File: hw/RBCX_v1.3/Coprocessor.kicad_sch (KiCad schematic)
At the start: 31 parts

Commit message: Work in progress
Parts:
- IC1: renamed from IC?; footprint RBCX:QFN50P400X400X95-24N -> Package_DFN_QFN:QFN-24-1EP_4x4mm_P0.5mm_EP2.7x2.6mm
- IC2: renamed from IC?; footprint RBCX:QFP50P1600X1600X160-100N_STM32F103VCT6 -> RBCX:LQFN100_14x14mm
- Y2: renamed from Y?; footprint RBCX:SMD-3215_2P -> Crystal:Crystal_SMD_3215-2Pin_3.2x1.5mm
- gave numbers to parts that had none: 28

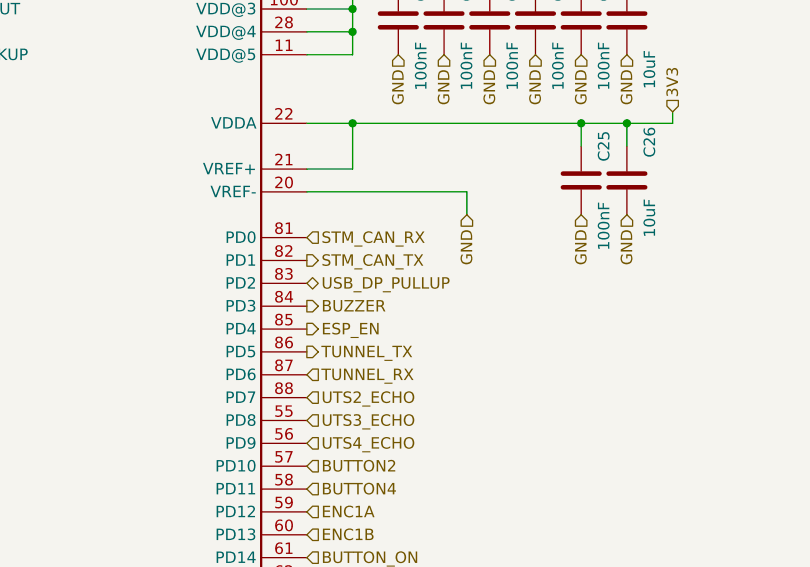
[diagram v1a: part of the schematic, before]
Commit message: New PCB layout
some changes of schema:
- change PD sink AO33772 to AO33771
- remove power switch
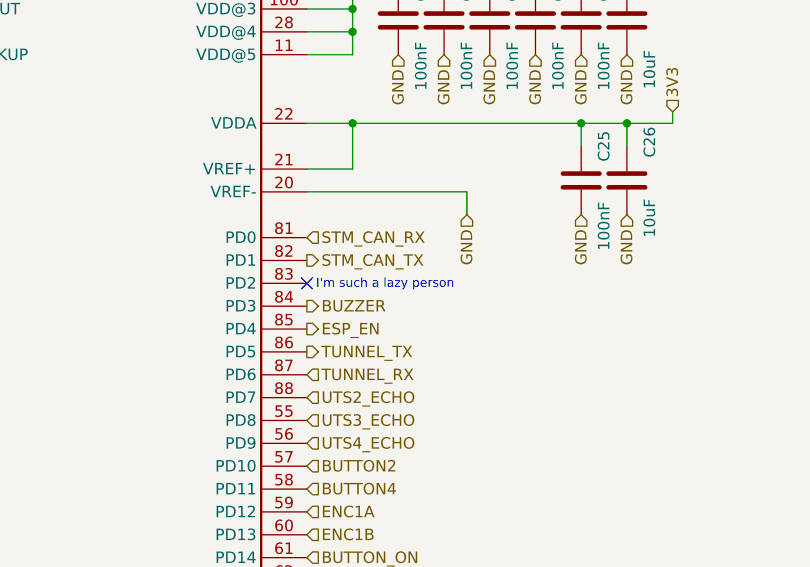
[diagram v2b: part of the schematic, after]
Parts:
- J34: footprint Connector_PinHeader_2.54mm:PinHeader_1x04_P2.54mm_Vertical -> RBCX:PinHeader_1x04_P2.54mm_Vertical
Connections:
- net USB_DP_PULLUP: no longer names the net of IC2.83 (PD2)
- no-connect marks 0 -> 1
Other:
- note added: "I'm such a lazy person"
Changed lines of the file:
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@@
   (junction (at 101.6 33.02) (diameter 0) (color 0 0 0 0)
   )
+  (no_connect (at 91.44 68.58))
   (wire (pts (xy 147.32 147.32) (xy 144.78 147.32))
     (stroke (width 0) (type default) (color 0 0 0 0))
@@
   (wire (pts (xy 116.84 35.56) (xy 116.84 33.02))
     (stroke (width 0) (type default) (color 0 0 0 0))
+  )
+  (text "I'm such a lazy person" (at 92.456 69.342 0)
+    (effects (font (size 1 1)) (justify left bottom))
   )
   (text "v1.3" (at 217.805 191.643 180)
@@
   )
   (hierarchical_label "PWM3B" (shape output) (at 91.44 137.16 0)
-    (effects (font (size 1.27 1.27)) (justify left))
-  )
-  (hierarchical_label "USB_DP_PULLUP" (shape bidirectional) (at 91.44 68.58 0)
     (effects (font (size 1.27 1.27)) (justify left))
   )
@@
       (effects (font (size 1.27 1.27)) (justify left))
     )
-    (property "Footprint" "Connector_PinHeader_2.54mm:PinHeader_1x04_P2.54mm_Vertical" (id 2) (at 243.84 97.79 0)
-      (effects (font (size 1.27 1.27)) hide)
-    )
+    (property "Footprint" "RBCX:PinHeader_1x04_P2.54mm_Vertical" (id 2) (at 243.84 97.79 0)
+      (effects (font (size 1.27 1.27)) hide)
+    )

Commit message: Production files
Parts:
- J34: JLCPCB_CORRECTION (none) -> 0;-3.81;90
- TP12: JLCPCB_IGNORE (none) -> 1
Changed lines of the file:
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@@
+      (effects (font (size 1.27 1.27)) hide)
+    )
+    (property "JLCPCB_IGNORE" "1" (id 4) (at 186.69 54.61 0)
       (effects (font (size 1.27 1.27)) hide)
     )
@@
       (effects (font (size 1.27 1.27)) hide)
     )
+    (property "JLCPCB_CORRECTION" "0;-3.81;90" (id 6) (at 243.84 97.79 0)
+      (effects (font (size 1.27 1.27)) hide)
+    )

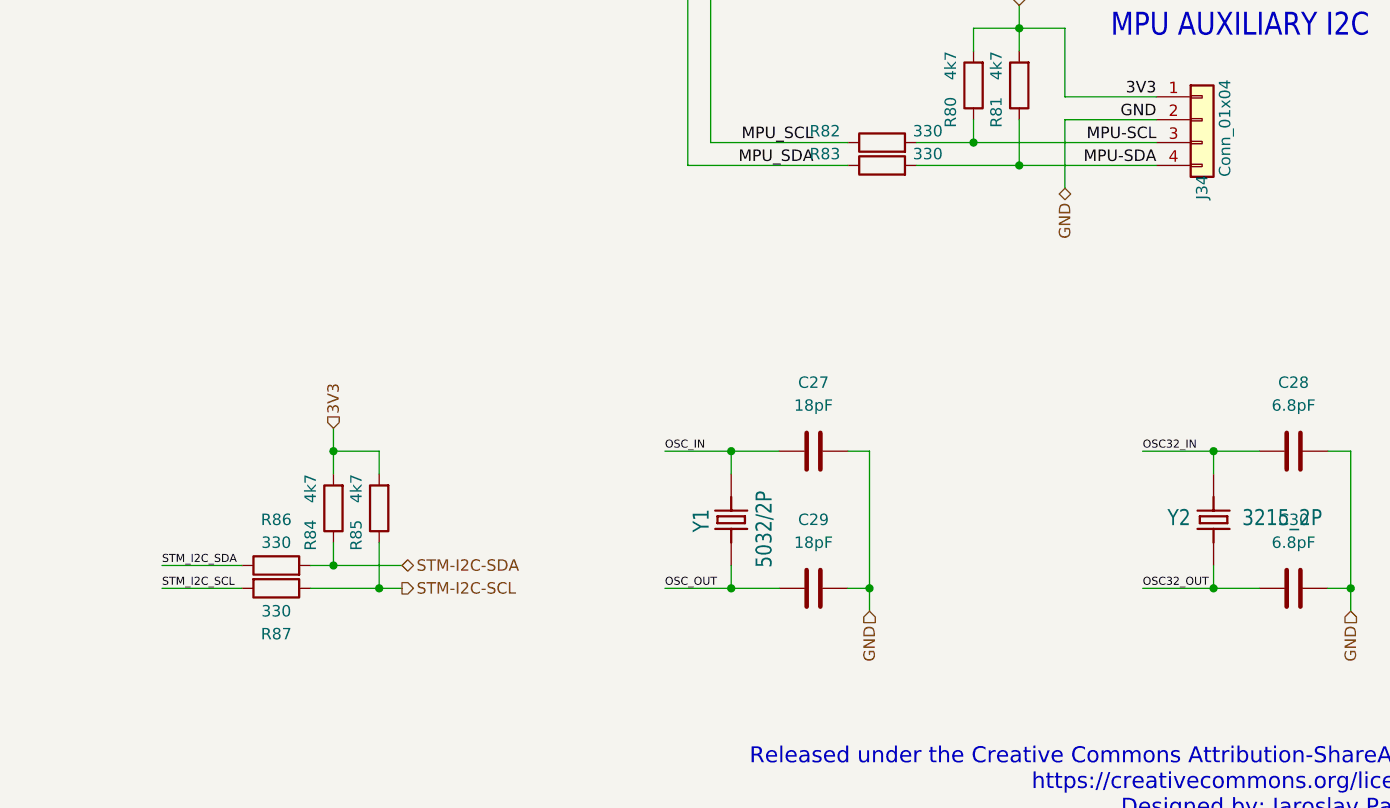
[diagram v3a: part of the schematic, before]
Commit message: Protective resistors for I2C on connectors
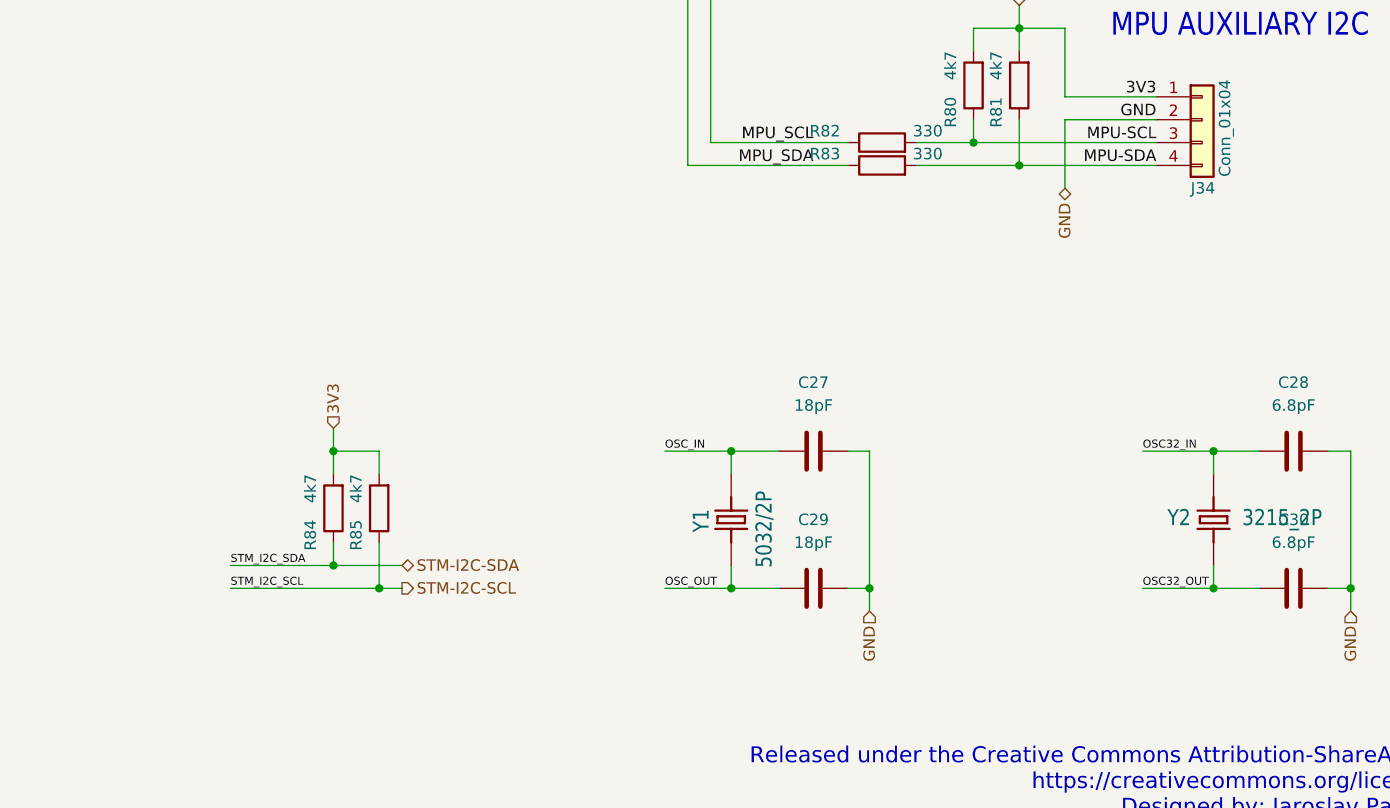
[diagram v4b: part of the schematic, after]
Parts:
- removed R86, R87: 330, Capacitor_SMD:C_0201_0603Metric, symbol Device:R
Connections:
- net STM_I2C_SCL is gone; now on net STM-I2C-SCL: IC1.23 (SCL), IC2.95 (PB8)
- net STM_I2C_SDA is gone; now on net STM-I2C-SDA: IC1.24 (SDA), IC2.96 (PB9)
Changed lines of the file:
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@@
   )
   (no_connect (at 91.44 68.58))
-  (wire (pts (xy 147.32 147.32) (xy 144.78 147.32))
+  (wire (pts (xy 135.89 147.32) (xy 147.32 147.32))
     (stroke (width 0) (type default) (color 0 0 0 0))
   )
@@
     (stroke (width 0) (type default) (color 0 0 0 0))
   )
-  (wire (pts (xy 137.16 149.86) (xy 128.27 149.86))
+  (wire (pts (xy 135.89 149.86) (xy 152.4 149.86))
     (stroke (width 0) (type default) (color 0 0 0 0))
   )
@@
     (stroke (width 0) (type default) (color 0 0 0 0))
   )
-  (wire (pts (xy 137.16 147.32) (xy 128.27 147.32))
-    (stroke (width 0) (type default) (color 0 0 0 0))
-  )
   (wire (pts (xy 45.72 167.64) (xy 36.83 167.64))
     (stroke (width 0) (type default) (color 0 0 0 0))
@@
   )
   (wire (pts (xy 228.6 97.79) (xy 228.6 105.41))
-    (stroke (width 0) (type default) (color 0 0 0 0))
-  )
-  (wire (pts (xy 152.4 149.86) (xy 144.78 149.86))
     (stroke (width 0) (type default) (color 0 0 0 0))
   )
@@
     (effects (font (size 1.27 1.27)) (justify right bottom))
   )
-  (label "STM_I2C_SCL" (at 128.27 149.86 0)
+  (label "STM_I2C_SCL" (at 135.89 149.86 0)
     (effects (font (size 0.889 0.889)) (justify left bottom))
   )
@@
     (effects (font (size 0.889 0.889)) (justify left bottom))
   )
-  (label "STM_I2C_SDA" (at 128.27 147.32 0)
+  (label "STM_I2C_SDA" (at 135.89 147.32 0)
     (effects (font (size 0.889 0.889)) (justify left bottom))
   )
@@
     )
     (property "Basic/Extended" "E" (id 5) (at 194.31 52.07 0)
-      (effects (font (size 1.27 1.27)) hide)
-    )
-    (pin "1")
-    (pin "2")
-  )
-  (symbol (lib_id "Device:R") (at 140.97 149.86 270) (unit 1)
-    (in_bom yes) (on_board yes)
-    (property "Reference" "R87" (id 0) (at 140.97 154.94 90))
-    (property "Value" "330" (id 1) (at 140.97 152.4 90))
-    (property "Footprint" "Capacitor_SMD:C_0201_0603Metric" (id 2) (at 140.97 148.082 90)
-      (effects (font (size 1.27 1.27)) hide)
-    )
-    (property "Datasheet" "~" (id 3) (at 140.97 149.86 0)
-      (effects (font (size 1.27 1.27)) hide)
-    )
-    (property "LCSC" "C473445" (id 4) (at 140.97 149.86 90)
-      (effects (font (size 1.27 1.27)) hide)
-    )
-    (property "Basic/Extended" "E" (id 5) (at 140.97 149.86 0)
       (effects (font (size 1.27 1.27)) hide)
     )
@@
     (pin "2")
   )
-  (symbol (lib_id "Device:R") (at 140.97 147.32 90) (unit 1)
-    (in_bom yes) (on_board yes)
-    (property "Reference" "R86" (id 0) (at 140.97 142.24 90))
-    (property "Value" "330" (id 1) (at 140.97 144.78 90))
-    (property "Footprint" "Capacitor_SMD:C_0201_0603Metric" (id 2) (at 140.97 149.098 90)
-      (effects (font (size 1.27 1.27)) hide)
-    )
-    (property "Datasheet" "~" (id 3) (at 140.97 147.32 0)
-      (effects (font (size 1.27 1.27)) hide)
-    )
-    (property "LCSC" "C473445" (id 4) (at 140.97 147.32 90)
-      (effects (font (size 1.27 1.27)) hide)
-    )
-    (property "Basic/Extended" "E" (id 5) (at 140.97 147.32 0)
-      (effects (font (size 1.27 1.27)) hide)
-    )
-    (pin "1")
-    (pin "2")
-  )
   (symbol (lib_id "Device:C") (at 254 134.62 90) (unit 1)
     (in_bom yes) (on_board yes) (fields_autoplaced)
@@
   (symbol (lib_id "Connector_Generic:Conn_01x04") (at 243.84 97.79 0) (unit 1)
     (in_bom yes) (on_board yes)
-    (property "Reference" "J34" (id 0) (at 243.84 106.68 90)
+    (property "Reference" "J34" (id 0) (at 242.57 105.41 0)
       (effects (font (size 1.27 1.27)) (justify left))
     )

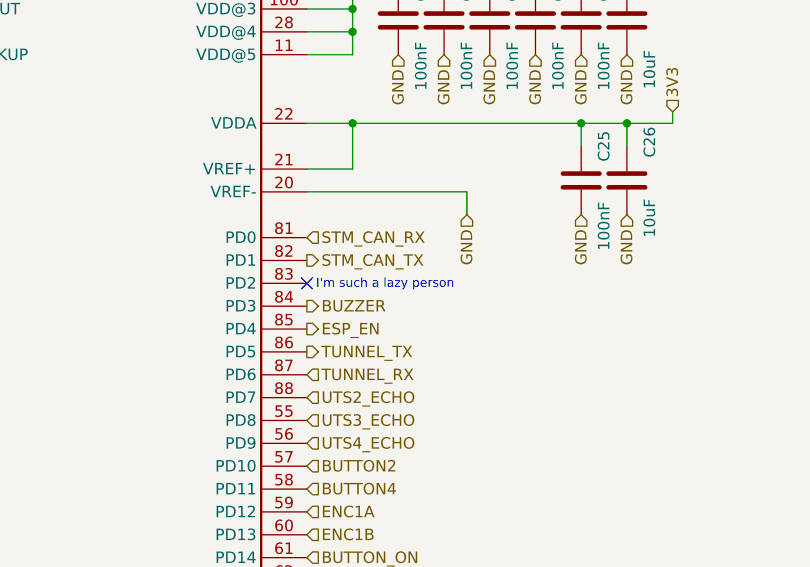
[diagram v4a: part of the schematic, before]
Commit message: Kuba issues
Change of power transistor from JSM3622 to JMSL0302AU

NTC connectors

Moving the Cell balancer behind the switch

and some little things
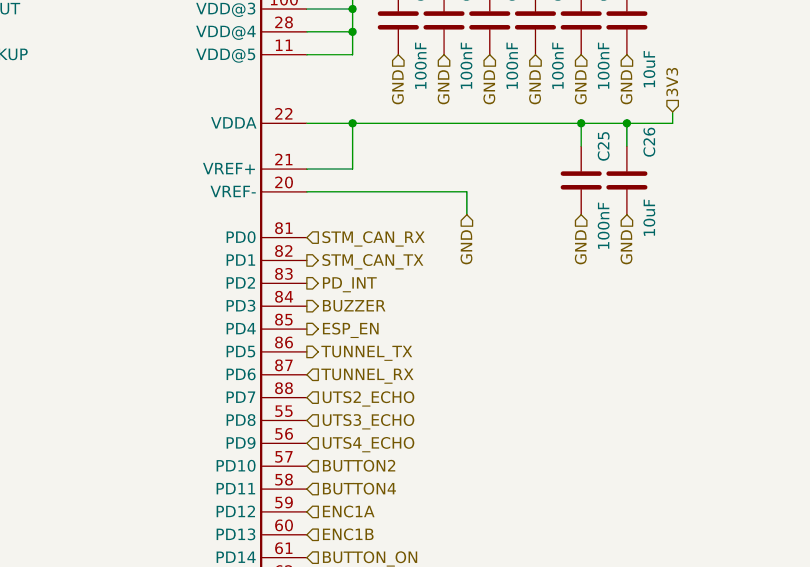
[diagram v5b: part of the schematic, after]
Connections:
- net PD_INT: now reaches IC2.83 (PD2)
- no-connect marks 1 -> 0
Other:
- note removed: "I'm such a lazy person"
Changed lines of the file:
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@@
   (junction (at 101.6 33.02) (diameter 0) (color 0 0 0 0)
   )
-  (no_connect (at 91.44 68.58))
   (wire (pts (xy 135.89 147.32) (xy 147.32 147.32))
     (stroke (width 0) (type default) (color 0 0 0 0))
@@
   (wire (pts (xy 116.84 35.56) (xy 116.84 33.02))
     (stroke (width 0) (type default) (color 0 0 0 0))
-  )
-  (text "I'm such a lazy person" (at 92.456 69.342 0)
-    (effects (font (size 1 1)) (justify left bottom))
   )
   (text "v1.3" (at 217.805 191.643 180)
@@
     (effects (font (size 1.27 1.27)) (justify right))
   )
+  (hierarchical_label "PD_INT" (shape output) (at 91.44 68.58 0)
+    (effects (font (size 1.27 1.27)) (justify left))
+  )
   (hierarchical_label "BUTTON_ON" (shape input) (at 91.44 99.06 0)
